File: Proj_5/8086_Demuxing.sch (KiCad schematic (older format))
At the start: 7 parts

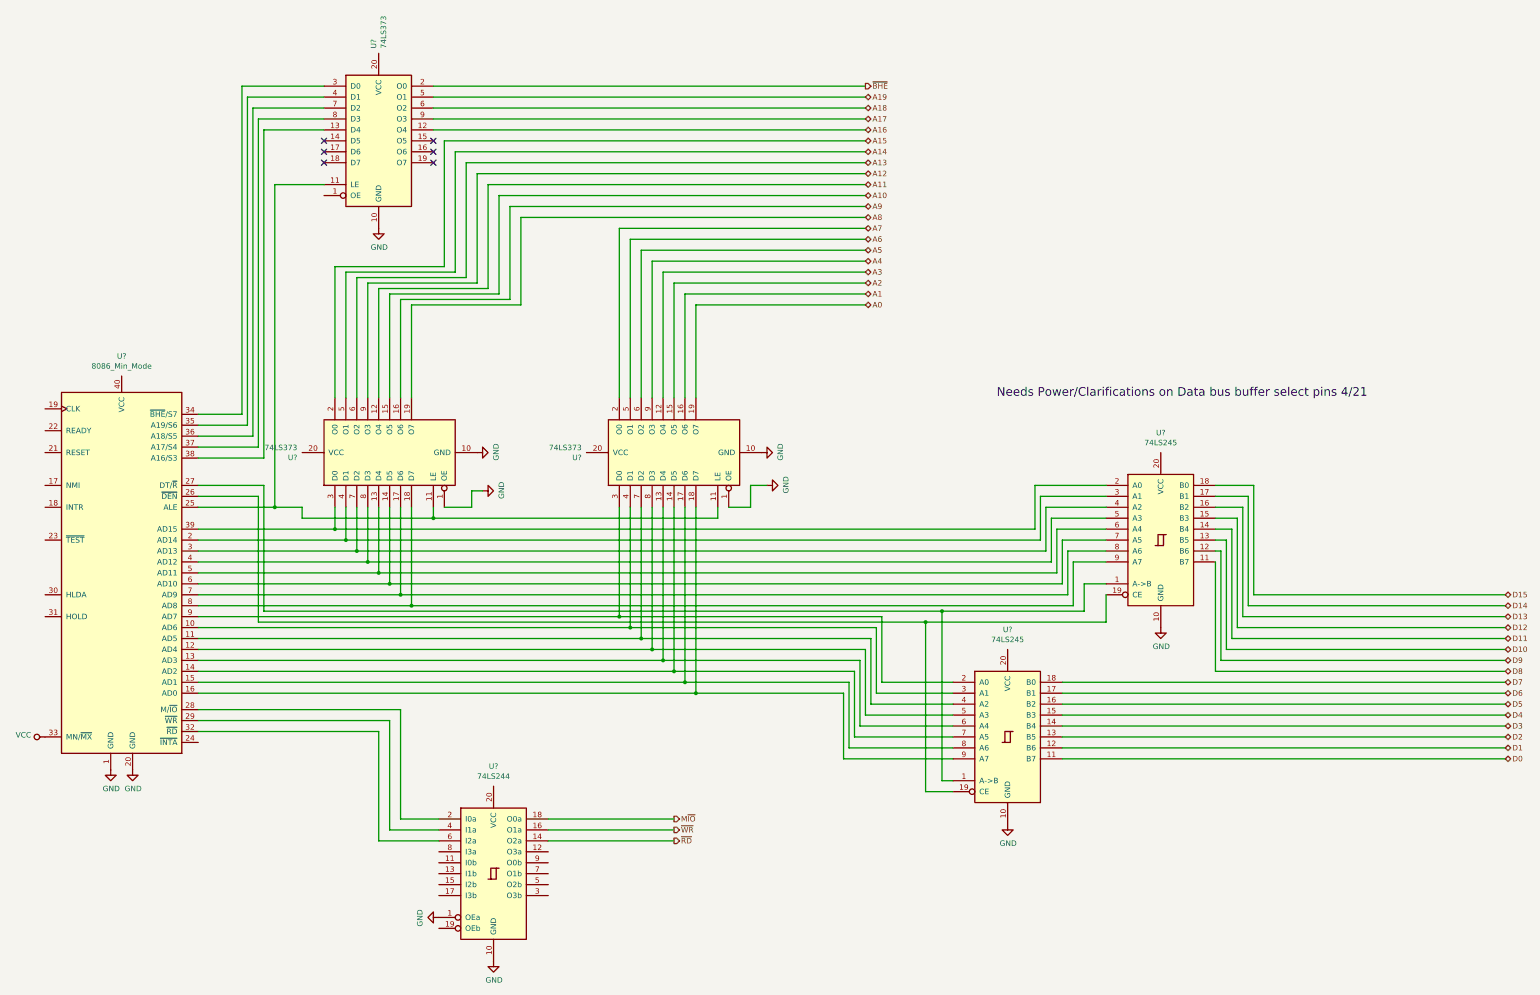
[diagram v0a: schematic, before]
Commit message: Added address decoding
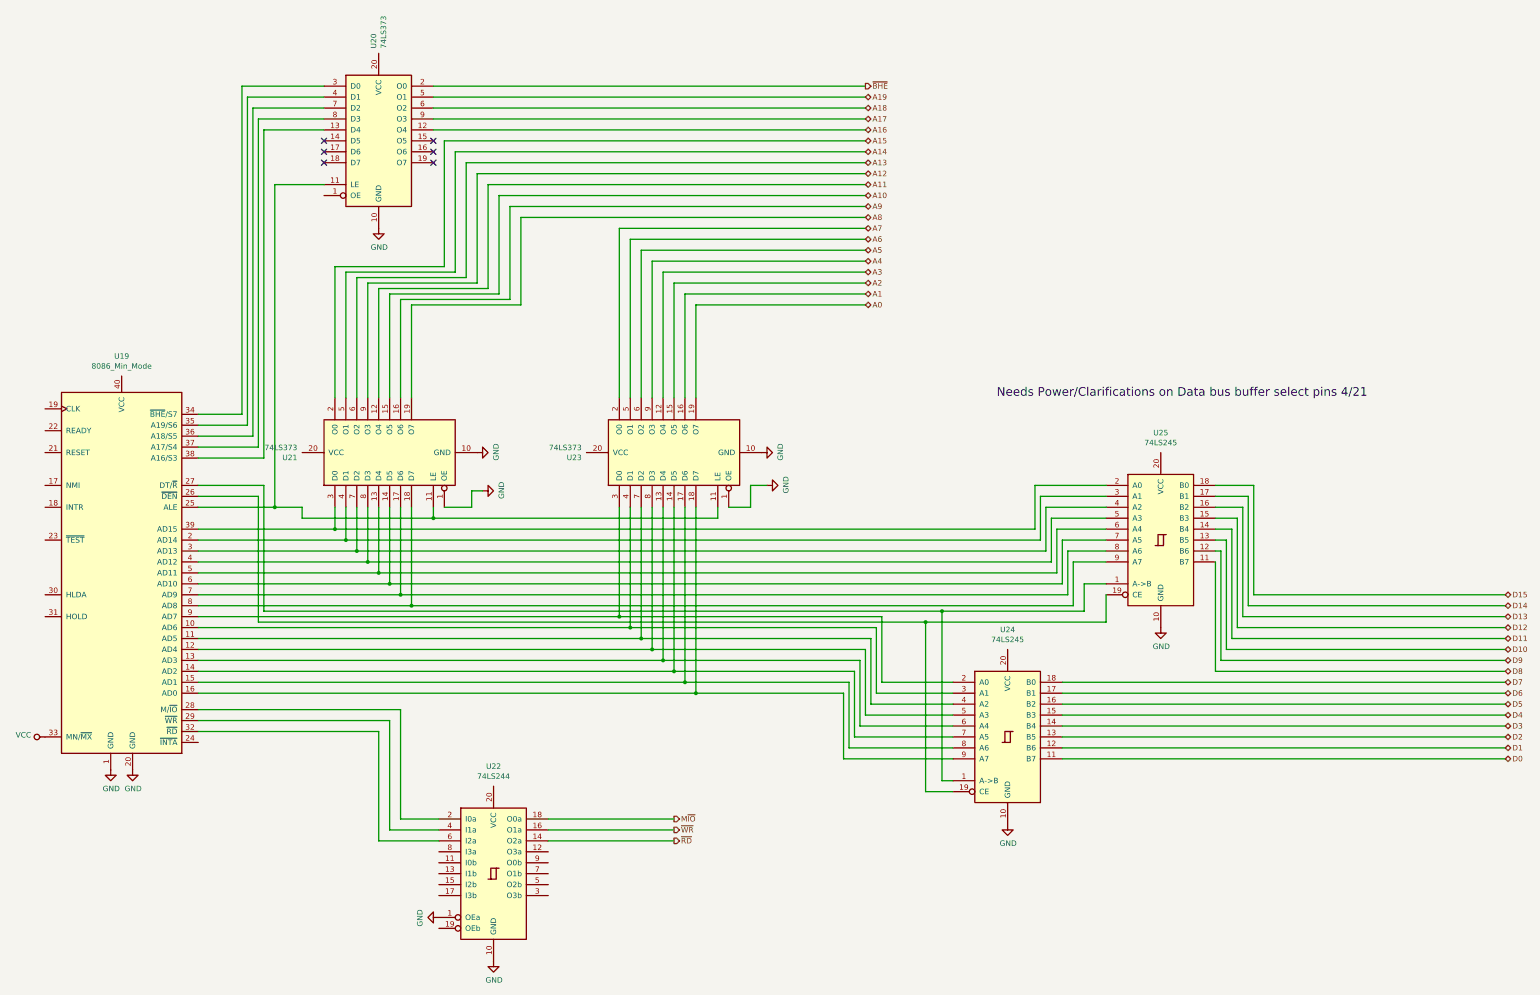
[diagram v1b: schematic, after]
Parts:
- gave numbers to parts that had none: 7
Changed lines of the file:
@@
 P 7850 8700
 AR Path="/5E9F413F" Ref="U?"  Part="1"
-AR Path="/5E9F3A3D/5E9F413F" Ref="U?"  Part="1"
-F 0 "U?" H 7850 10681 50  0000 C CNN
+AR Path="/5E9F3A3D/5E9F413F" Ref="U19"  Part="1"
+F 0 "U19" H 7850 10681 50  0000 C CNN
 F 1 "8086_Min_Mode" H 7850 10590 50  0000 C CNN
 F 2 "Package_DIP:DIP-40_W15.24mm" H 7900 8800 50  0001 C CIN
@@
 $EndComp
 $Comp
-L 74xx:74LS373 U?
+L 74xx:74LS373 U23
 U 1 1 5E9F8AC2
 P 12900 7600
-F 0 "U?" V 12854 8444 50  0000 L CNN
+F 0 "U23" V 12854 8444 50  0000 L CNN
 F 1 "74LS373" V 12945 8444 50  0000 L CNN
 F 2 "" H 12900 7600 50  0001 C CNN
@@
 $EndComp
 $Comp
-L 74xx:74LS373 U?
+L 74xx:74LS373 U20
 U 1 1 5E9FCB3B
 P 10200 4750
-F 0 "U?" V 10154 5594 50  0000 L CNN
+F 0 "U20" V 10154 5594 50  0000 L CNN
 F 1 "74LS373" V 10245 5594 50  0000 L CNN
 F 2 "" H 10200 4750 50  0001 C CNN
@@
 $EndComp
 $Comp
-L 74xx:74LS245 U?
+L 74xx:74LS245 U25
 U 1 1 5EA00484
 P 17350 8400
-F 0 "U?" H 17350 9381 50  0000 C CNN
+F 0 "U25" H 17350 9381 50  0000 C CNN
 F 1 "74LS245" H 17350 9290 50  0000 C CNN
 F 2 "" H 17350 8400 50  0001 C CNN
@@
 $EndComp
 $Comp
-L 74xx:74LS245 U?
+L 74xx:74LS245 U24
 U 1 1 5EA0390A
 P 15950 10200
-F 0 "U?" H 15950 11181 50  0000 C CNN
+F 0 "U24" H 15950 11181 50  0000 C CNN
 F 1 "74LS245" H 15950 11090 50  0000 C CNN
 F 2 "" H 15950 10200 50  0001 C CNN
@@
 $EndComp
 $Comp
-L 74xx:74LS244 U?
+L 74xx:74LS244 U22
 U 1 1 5EA03AD7
 P 11250 11450
-F 0 "U?" H 11250 12431 50  0000 C CNN
+F 0 "U22" H 11250 12431 50  0000 C CNN
 F 1 "74LS244" H 11250 12340 50  0000 C CNN
 F 2 "" H 11250 11450 50  0001 C CNN
@@
 $EndComp
 $Comp
-L 74xx:74LS373 U?
+L 74xx:74LS373 U21
 U 1 1 5E9FBE84
 P 10300 7600
-F 0 "U?" V 10254 8444 50  0000 L CNN
+F 0 "U21" V 10254 8444 50  0000 L CNN
 F 1 "74LS373" V 10345 8444 50  0000 L CNN
 F 2 "" H 10300 7600 50  0001 C CNN
@@
 	9800 8300 9800 8100
 $Comp
-L power:GND #PWR?
+L power:GND #PWR0116
 U 1 1 5EA0E391
 P 10200 5550
-F 0 "#PWR?" H 10200 5300 50  0001 C CNN
+F 0 "#PWR0116" H 10200 5300 50  0001 C CNN
 F 1 "GND" H 10205 5377 50  0000 C CNN
 F 2 "" H 10200 5550 50  0001 C CNN
@@
 $EndComp
 $Comp
-L power:GND #PWR?
+L power:GND #PWR0117
 U 1 1 5EA0EF94
 P 11100 7600
-F 0 "#PWR?" H 11100 7350 50  0001 C CNN
+F 0 "#PWR0117" H 11100 7350 50  0001 C CNN
 F 1 "GND" H 11105 7427 50  0000 C CNN
 F 2 "" H 11100 7600 50  0001 C CNN
@@
 $EndComp
 $Comp
-L power:GND #PWR?
+L power:GND #PWR0118
 U 1 1 5EA10035
 P 13700 7600
-F 0 "#PWR?" H 13700 7350 50  0001 C CNN
+F 0 "#PWR0118" H 13700 7350 50  0001 C CNN
 F 1 "GND" H 13705 7427 50  0000 C CNN
 F 2 "" H 13700 7600 50  0001 C CNN
@@
 $EndComp
 $Comp
-L power:GND #PWR?
+L power:GND #PWR0119
 U 1 1 5EA120BD
 P 7950 10500
-F 0 "#PWR?" H 7950 10250 50  0001 C CNN
+F 0 "#PWR0119" H 7950 10250 50  0001 C CNN
 F 1 "GND" H 7955 10327 50  0000 C CNN
 F 2 "" H 7950 10500 50  0001 C CNN
@@
 $EndComp
 $Comp
-L power:GND #PWR?
+L power:GND #PWR0120
 U 1 1 5EA1307D
 P 7750 10500
-F 0 "#PWR?" H 7750 10250 50  0001 C CNN
+F 0 "#PWR0120" H 7750 10250 50  0001 C CNN
 F 1 "GND" H 7755 10327 50  0000 C CNN
 F 2 "" H 7750 10500 50  0001 C CNN
@@
 ~BHE
 $Comp
-L power:GND #PWR?
+L power:GND #PWR0121
 U 1 1 5EBC880F
 P 15950 11000
-F 0 "#PWR?" H 15950 10750 50  0001 C CNN
+F 0 "#PWR0121" H 15950 10750 50  0001 C CNN
 F 1 "GND" H 15955 10827 50  0000 C CNN
 F 2 "" H 15950 11000 50  0001 C CNN
@@
 	9150 9050 15350 9050
 $Comp
-L power:GND #PWR?
+L power:GND #PWR0122
 U 1 1 5EBD1B0F
 P 17350 9200
-F 0 "#PWR?" H 17350 8950 50  0001 C CNN
+F 0 "#PWR0122" H 17350 8950 50  0001 C CNN
 F 1 "GND" H 17355 9027 50  0000 C CNN
 F 2 "" H 17350 9200 50  0001 C CNN
@@
 $EndComp
 $Comp
-L power:GND #PWR?
+L power:GND #PWR0123
 U 1 1 5EBDAA8F
 P 11250 12250
-F 0 "#PWR?" H 11250 12000 50  0001 C CNN
+F 0 "#PWR0123" H 11250 12000 50  0001 C CNN
 F 1 "GND" H 11255 12077 50  0000 C CNN
 F 2 "" H 11250 12250 50  0001 C CNN
@@
 $EndComp
 $Comp
-L power:VCC #PWR?
+L power:VCC #PWR0124
 U 1 1 5EBF8953
 P 7150 10200
-F 0 "#PWR?" H 7150 10050 50  0001 C CNN
+F 0 "#PWR0124" H 7150 10050 50  0001 C CNN
 F 1 "VCC" V 7168 10327 50  0000 L CNN
 F 2 "" H 7150 10200 50  0001 C CNN
@@
 	13600 7900 13750 7900
 $Comp
-L power:GND #PWR?
+L power:GND #PWR0125
 U 1 1 5EC366D7
 P 13750 7900
-F 0 "#PWR?" H 13750 7650 50  0001 C CNN
+F 0 "#PWR0125" H 13750 7650 50  0001 C CNN
 F 1 "GND" H 13755 7727 50  0000 C CNN
 F 2 "" H 13750 7900 50  0001 C CNN
@@
 $EndComp
 $Comp
-L power:GND #PWR?
+L power:GND #PWR0126
 U 1 1 5EC40EB5
 P 11150 7950
-F 0 "#PWR?" H 11150 7700 50  0001 C CNN
+F 0 "#PWR0126" H 11150 7700 50  0001 C CNN
 F 1 "GND" H 11155 7777 50  0000 C CNN
 F 2 "" H 11150 7950 50  0001 C CNN
@@
 ~RD
 $Comp
-L power:GND #PWR?
+L power:GND #PWR0127
 U 1 1 5ECB05B8
 P 10750 11850
-F 0 "#PWR?" H 10750 11600 50  0001 C CNN
+F 0 "#PWR0127" H 10750 11600 50  0001 C CNN
 F 1 "GND" H 10755 11677 50  0000 C CNN
 F 2 "" H 10750 11850 50  0001 C CNN

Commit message: Added some connections; Some connections are reporting 'No connections' and IDK why
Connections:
- net CLK: now reaches U19.19 (CLK)
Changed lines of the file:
@@
 	0    1    1    0
 $EndComp
+Text HLabel 7150 7200 0    50   Input ~ 0
+CLK
 $EndSCHEMATC

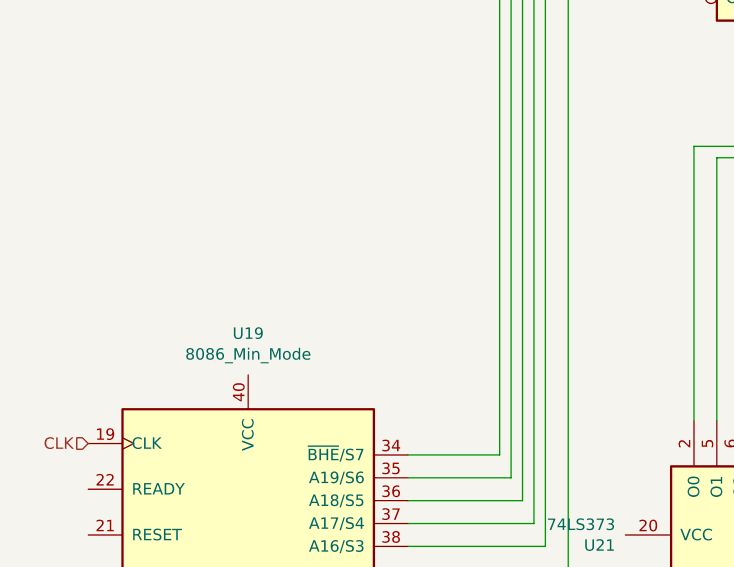
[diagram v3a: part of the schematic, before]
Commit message: Added Caps to Each Vcc per desc.
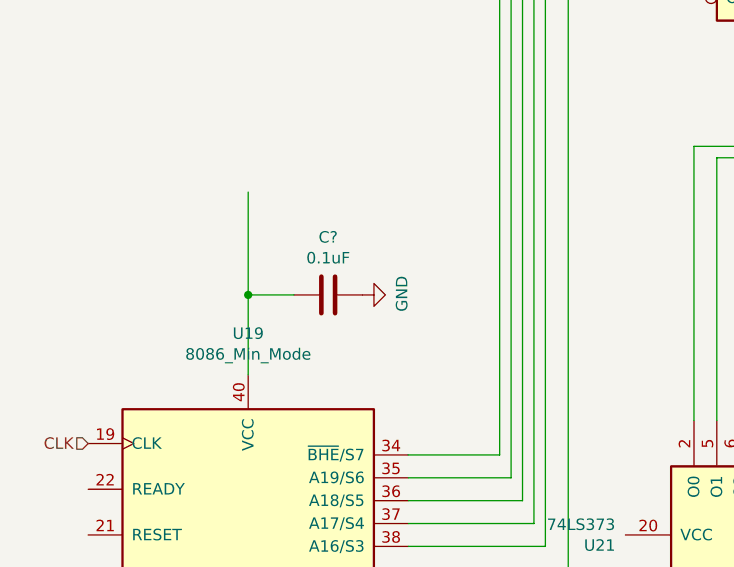
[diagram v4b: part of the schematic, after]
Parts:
- added C?: 0.1uF, symbol Device:C
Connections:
- net GND: now also C?.1
- net at U19.40 (VCC): now also C?.2
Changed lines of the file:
@@
 Text HLabel 7150 7200 0    50   Input ~ 0
 CLK
+$Comp
+L Device:C C?
+U 1 1 5EA54382
+P 8200 6550
+AR Path="/5EA98353/5EA54382" Ref="C?"  Part="1"
+AR Path="/5E9F3A3D/5EA54382" Ref="C?"  Part="1"
+F 0 "C?" V 7948 6550 50  0000 C CNN
+F 1 "0.1uF" V 8039 6550 50  0000 C CNN
+F 2 "" H 8238 6400 50  0001 C CNN
+F 3 "~" H 8200 6550 50  0001 C CNN
+	1    8200 6550
+	0    1    1    0
+$EndComp
+Wire Wire Line
+	8050 6550 7850 6550
+Wire Wire Line
+	7850 6550 7850 6900
+Wire Wire Line
+	7850 6100 7850 6550
+Connection ~ 7850 6550
+$Comp
+L power:GND #PWR?
+U 1 1 5EA86357
+P 8350 6550
+F 0 "#PWR?" H 8350 6300 50  0001 C CNN
+F 1 "GND" H 8355 6377 50  0000 C CNN
+F 2 "" H 8350 6550 50  0001 C CNN
+F 3 "" H 8350 6550 50  0001 C CNN
+	1    8350 6550
+	0    -1   -1   0
+$EndComp
 $EndSCHEMATC

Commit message: Hey
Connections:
- net RESET: now reaches U19.21 (RESET)
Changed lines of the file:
@@
 	0    -1   -1   0
 $EndComp
+Text HLabel 7150 7600 0    50   Input ~ 0
+RESET
 $EndSCHEMATC
